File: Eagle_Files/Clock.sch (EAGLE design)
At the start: 23 parts, among them IC1 MEGA8-AI, IC2 DS3231/SO, X1 332-02

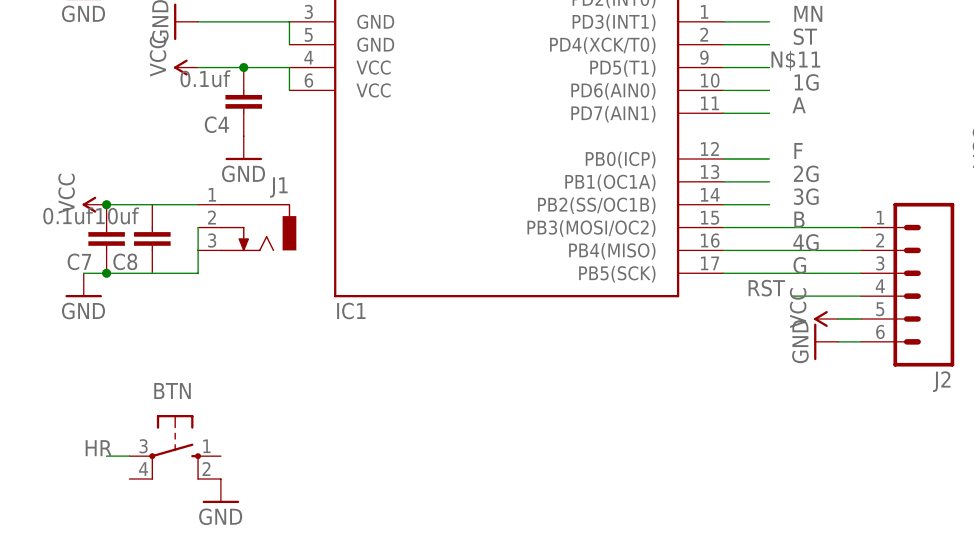
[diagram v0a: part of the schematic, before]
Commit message: Adding usb connector intead of DC jack
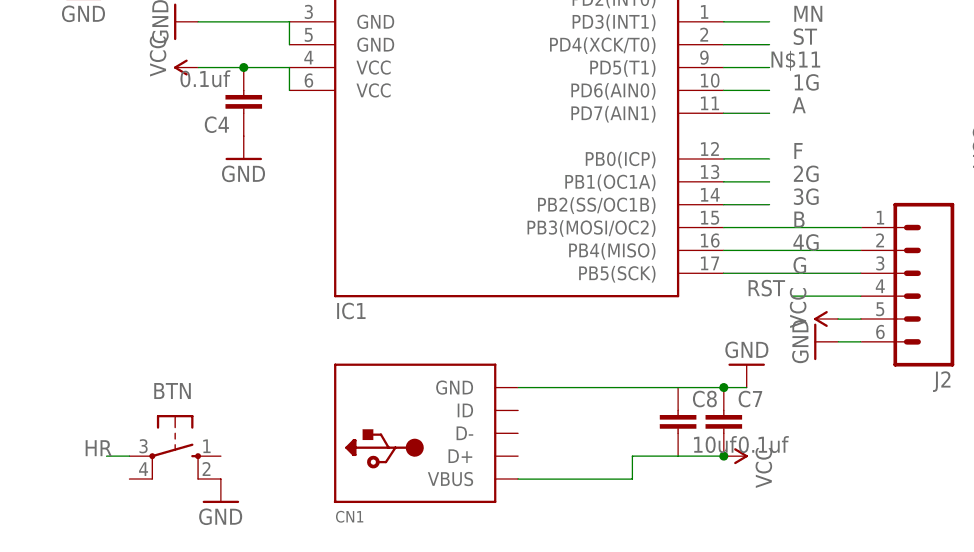
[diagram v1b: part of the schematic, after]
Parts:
- removed J1: (no value), con-jack:DCJ0303
- added CN1: (no value), adafruit:USBMINIB
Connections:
- net GND: now also CN1.GND; no longer J1.2, J1.3
- net VCC: now also CN1.VBUS; no longer J1.1
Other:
- moved on the sheet: C7, C8
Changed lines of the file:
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@@
 <?xml version="1.0" encoding="utf-8"?>
 <!DOCTYPE eagle SYSTEM "eagle.dtd">
-<eagle version="7.4.0">
+<eagle version="8.2.2">
 <drawing>
 <settings>
@@
 </classes>
 <parts>
-<part name="IC1" library="atmel" deviceset="MEGA8" device="-AI"/>
+<part name="IC1" library="atmel" library_urn="urn:adsk.eagle:library:105" deviceset="MEGA8" device="-AI"/>
 <part name="Q1" library="adafruit" deviceset="CRYSTAL" device="HC49S"/>
-<part name="C1" library="rcl" deviceset="C-EU" device="C0603" value="22pf"/>
-<part name="C2" library="rcl" deviceset="C-EU" device="C0603" value="22pf"/>
+<part name="C1" library="rcl" library_urn="urn:adsk.eagle:library:334" deviceset="C-EU" device="C0603" value="22pf"/>
+<part name="C2" library="rcl" library_urn="urn:adsk.eagle:library:334" deviceset="C-EU" device="C0603" value="22pf"/>
 <part name="R1" library="adafruit" deviceset="R-US_" device="R0603" value="10K"/>
 <part name="GND11" library="SparkFun-Aesthetics" deviceset="GND" device=""/>
@@
 <part name="SUPPLY8" library="SparkFun-Aesthetics" deviceset="VCC" device=""/>
 <part name="GND1" library="SparkFun-Aesthetics" deviceset="GND" device=""/>
-<part name="BTN" library="switch-omron" deviceset="10-XX" device=""/>
+<part name="BTN" library="switch-omron" library_urn="urn:adsk.eagle:library:377" deviceset="10-XX" device=""/>
 <part name="R2" library="adafruit" deviceset="R-US_" device="R0603" value="1k"/>
 <part name="R3" library="adafruit" deviceset="R-US_" device="R0603" value="1k"/>
@@
 <part name="U$1" library="ram_86" deviceset="7SEG" device="7SEG12"/>
 <part name="IC2" library="adafruit" deviceset="DS3231" device="/SO"/>
-<part name="C3" library="rcl" deviceset="C-EU" device="C0603" value="0.1uf"/>
+<part name="C3" library="rcl" library_urn="urn:adsk.eagle:library:334" deviceset="C-EU" device="C0603" value="0.1uf"/>
 <part name="GND4" library="SparkFun-Aesthetics" deviceset="GND" device=""/>
 <part name="SUPPLY2" library="SparkFun-Aesthetics" deviceset="VCC" device=""/>
 <part name="GND6" library="SparkFun-Aesthetics" deviceset="GND" device=""/>
-<part name="C4" library="rcl" deviceset="C-EU" device="C0603" value="0.1uf"/>
-<part name="C5" library="rcl" deviceset="C-EU" device="C0603" value="0.1uf"/>
-<part name="C7" library="rcl" deviceset="C-EU" device="C0603" value="0.1uf"/>
-<part name="C8" library="rcl" deviceset="C-EU" device="C0603" value="10uf"/>
+<part name="C4" library="rcl" library_urn="urn:adsk.eagle:library:334" deviceset="C-EU" device="C0603" value="0.1uf"/>
+<part name="C5" library="rcl" library_urn="urn:adsk.eagle:library:334" deviceset="C-EU" device="C0603" value="0.1uf"/>
+<part name="C7" library="rcl" library_urn="urn:adsk.eagle:library:334" deviceset="C-EU" device="C0603" value="0.1uf"/>
+<part name="C8" library="rcl" library_urn="urn:adsk.eagle:library:334" deviceset="C-EU" device="C0603" value="10uf"/>
 <part name="GND8" library="SparkFun-Aesthetics" deviceset="GND" device=""/>
 <part name="GND10" library="SparkFun-Aesthetics" deviceset="GND" device=""/>
@@
 <part name="SUPPLY5" library="SparkFun-Aesthetics" deviceset="VCC" device=""/>
 <part name="GND13" library="SparkFun-Aesthetics" deviceset="GND" device=""/>
-<part name="J1" library="con-jack" deviceset="DCJ0303" device=""/>
 <part name="J2" library="SparkFun-Connectors" deviceset="M06" device="LOCK_LONGPADS"/>
-<part name="X1" library="con-garry" deviceset="332-02" device=""/>
-<part name="DBG" library="con-garry" deviceset="332-02" device="" value=""/>
-<part name="FRAME1" library="frames" deviceset="DINA5_L" device=""/>
+<part name="X1" library="con-garry" library_urn="urn:adsk.eagle:library:147" deviceset="332-02" device=""/>
+<part name="DBG" library="con-garry" library_urn="urn:adsk.eagle:library:147" deviceset="332-02" device="" value=""/>
+<part name="FRAME1" library="frames" library_urn="urn:adsk.eagle:library:229" deviceset="DINA5_L" device=""/>
+<part name="CN1" library="adafruit" deviceset="USB" device="MINIB"/>
 </parts>
 <sheets>
@@
 <instance part="SUPPLY6" gate="G$1" x="10.16" y="25.4"/>
 <instance part="SUPPLY7" gate="G$1" x="27.94" y="-10.16" rot="R90"/>
-<instance part="GND5" gate="1" x="15.24" y="-35.56"/>
+<instance part="GND5" gate="1" x="88.9" y="-43.18" rot="R180"/>
 <instance part="GND12" gate="1" x="35.56" y="17.78"/>
 <instance part="SUPPLY8" gate="G$1" x="22.86" y="15.24" rot="R90"/>
@@
 <instance part="R4" gate="G$1" x="162.56" y="7.62"/>
 <instance part="R5" gate="G$1" x="162.56" y="22.86"/>
-<instance part="SUPPLY1" gate="G$1" x="17.78" y="-25.4" rot="R90"/>
+<instance part="SUPPLY1" gate="G$1" x="86.36" y="-53.34" rot="R270"/>
 <instance part="U$1" gate="G$1" x="142.875" y="10.795" rot="R270"/>
 <instance part="IC2" gate="G$1" x="142.24" y="-27.94"/>
@@
 <instance part="C4" gate="G$1" x="33.02" y="-15.24" rot="R180"/>
 <instance part="C5" gate="G$1" x="30.48" y="17.78" rot="R180"/>
-<instance part="C7" gate="G$1" x="17.78" y="-30.48" rot="R180"/>
-<instance part="C8" gate="G$1" x="22.86" y="-30.48" rot="R180"/>
+<instance part="C7" gate="G$1" x="86.36" y="-48.26"/>
+<instance part="C8" gate="G$1" x="81.28" y="-48.26"/>
 <instance part="GND8" gate="1" x="27.94" y="22.86" rot="R270"/>
 <instance part="GND10" gate="1" x="33.02" y="-20.32"/>
@@
 <instance part="SUPPLY5" gate="G$1" x="99.06" y="-38.1" rot="R90"/>
 <instance part="GND13" gate="1" x="96.52" y="-40.64" rot="R270"/>
-<instance part="J1" gate="G$1" x="35.56" y="-27.94" rot="MR0"/>
 <instance part="J2" gate="G$1" x="106.68" y="-33.02" rot="R180"/>
 <instance part="X1" gate="-1" x="160.02" y="-22.86"/>
@@
 <attribute name="LAST_DATE_TIME" x="140.97" y="-73.66" size="2.286" layer="94"/>
 </instance>
+<instance part="CN1" gate="G$1" x="53.34" y="-50.8" rot="MR180"/>
 </instances>
 <busses>
@@
 <segment>
 <pinref part="GND5" gate="1" pin="GND"/>
-<wire x1="15.24" y1="-33.02" x2="17.78" y2="-33.02" width="0.1524" layer="91"/>
+<wire x1="88.9" y1="-45.72" x2="86.36" y2="-45.72" width="0.1524" layer="91"/>
 <pinref part="C7" gate="G$1" pin="1"/>
-<wire x1="17.78" y1="-33.02" x2="22.86" y2="-33.02" width="0.1524" layer="91"/>
-<junction x="17.78" y="-33.02"/>
+<wire x1="86.36" y1="-45.72" x2="81.28" y2="-45.72" width="0.1524" layer="91"/>
+<junction x="86.36" y="-45.72"/>
 <pinref part="C8" gate="G$1" pin="1"/>
-<pinref part="J1" gate="G$1" pin="3"/>
-<wire x1="27.94" y1="-30.48" x2="27.94" y2="-33.02" width="0.1524" layer="91"/>
-<wire x1="27.94" y1="-33.02" x2="22.86" y2="-33.02" width="0.1524" layer="91"/>
-<pinref part="J1" gate="G$1" pin="2"/>
-<wire x1="27.94" y1="-30.48" x2="27.94" y2="-27.94" width="0.1524" layer="91"/>
+<wire x1="81.28" y1="-45.72" x2="63.5" y2="-45.72" width="0.1524" layer="91"/>
+<pinref part="CN1" gate="G$1" pin="GND"/>
 </segment>
 <segment>
@@
 <segment>
 <pinref part="C7" gate="G$1" pin="2"/>
-<wire x1="17.78" y1="-25.4" x2="22.86" y2="-25.4" width="0.1524" layer="91"/>
+<wire x1="86.36" y1="-53.34" x2="81.28" y2="-53.34" width="0.1524" layer="91"/>
 <pinref part="C8" gate="G$1" pin="2"/>
-<pinref part="J1" gate="G$1" pin="1"/>
-<wire x1="22.86" y1="-25.4" x2="27.94" y2="-25.4" width="0.1524" layer="91"/>
 <pinref part="SUPPLY1" gate="G$1" pin="VCC"/>
-<junction x="17.78" y="-25.4"/>
+<junction x="86.36" y="-53.34"/>
+<pinref part="CN1" gate="G$1" pin="VBUS"/>
+<wire x1="63.5" y1="-55.88" x2="76.2" y2="-55.88" width="0.1524" layer="91"/>
+<wire x1="76.2" y1="-55.88" x2="76.2" y2="-53.34" width="0.1524" layer="91"/>
+<wire x1="76.2" y1="-53.34" x2="81.28" y2="-53.34" width="0.1524" layer="91"/>
 </segment>
 </net>
@@
 </schematic>
 </drawing>
+<compatibility>
+<note version="8.2" severity="warning">
+Since Version 8.2, Eagle supports online libraries. The ids
+of those online libraries will not be understood (or retained)
+with this version.
+</note>
+</compatibility>
 </eagle>
